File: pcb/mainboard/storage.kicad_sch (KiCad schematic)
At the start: 0 parts

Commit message: - Upgrade KiCad to latest version - Working on PM circuits - Initial USB Type-C support - Initial support for LCD
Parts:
- added C?: 100nF, Capacitor_SMD:C_0201_0603Metric, symbol Device:C
- added C?: 22uF, Capacitor_SMD:C_0603_1608Metric, symbol Device:C
- added C?: 470nF, Capacitor_SMD:C_0201_0603Metric, symbol Device:C
- added CARD?: MICRO_SD(TFC-WPAPR-08), footprint:TFC-WPAPR-08, symbol symbols:MICRO_SD(TFC-WPAPR-08)
- added J?: Bus_M.2_Socket_B, footprints:M2_BKEY, symbol Connector:Bus_M.2_Socket_B
- added R?: 100K, Capacitor_SMD:C_0402_1005Metric, symbol Device:R
- added R?: 0, Resistor_SMD:R_0402_1005Metric, symbol Device:R
- added U?: W25Q128JVP, Package_SON:WSON-8-1EP_6x5mm_P1.27mm_EP3.4x4.3mm, symbol Memory_Flash:W25Q32JVZP
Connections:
- new net: J?.11 (GND), J?.27 (GND), J?.3 (GND), J?.33 (GND), J?.39 (GND), J?.45 (GND), J?.5 (GND), J?.51 (GND), J?.57 (GND), J?.71 (GND), J?.73 (GND)
- new net: J?.2 (3.3V), J?.4 (3.3V), J?.70 (3.3V), J?.72 (3.3V), J?.74 (3.3V)
- new net: CARD?.5 (CLK/SCLK), R?.1
- new net +3V3: C?.1, C?.1, C?.2, CARD?.4 (VDD), R?.1, U?.8 (VCC)
- new net FSPI_1A_CS: R?.2, U?.1 (~CS)
- new net FSPI_1A_D0: U?.5 (DI(IO0))
- new net FSPI_1A_D1: U?.2 (DO(IO1))
- new net FSPI_1A_D2: U?.3 (IO2)
- new net FSPI_1A_D3: U?.7 (IO3)
- new net FSPI_1A_SCK: U?.6 (CLK)
- new net GND: C?.1, C?.2, C?.2, CARD?.10, CARD?.11, CARD?.12, CARD?.13, CARD?.6 (VSS), U?.4 (GND), U?.9 (EP)
- new net SD_CLK: R?.2
- new net SD_CMD: CARD?.3 (CMD/DI)
- new net SD_D0: CARD?.7 (DAT0/DO)
- new net SD_D1: CARD?.8 (DAT1/RES)
- new net SD_D2: CARD?.1 (DAT2/RES)
- new net SD_D3: CARD?.2 (CD/DAT3/CS)
- no-connect marks 0 -> 1
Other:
- note added: "Place close to MCU"

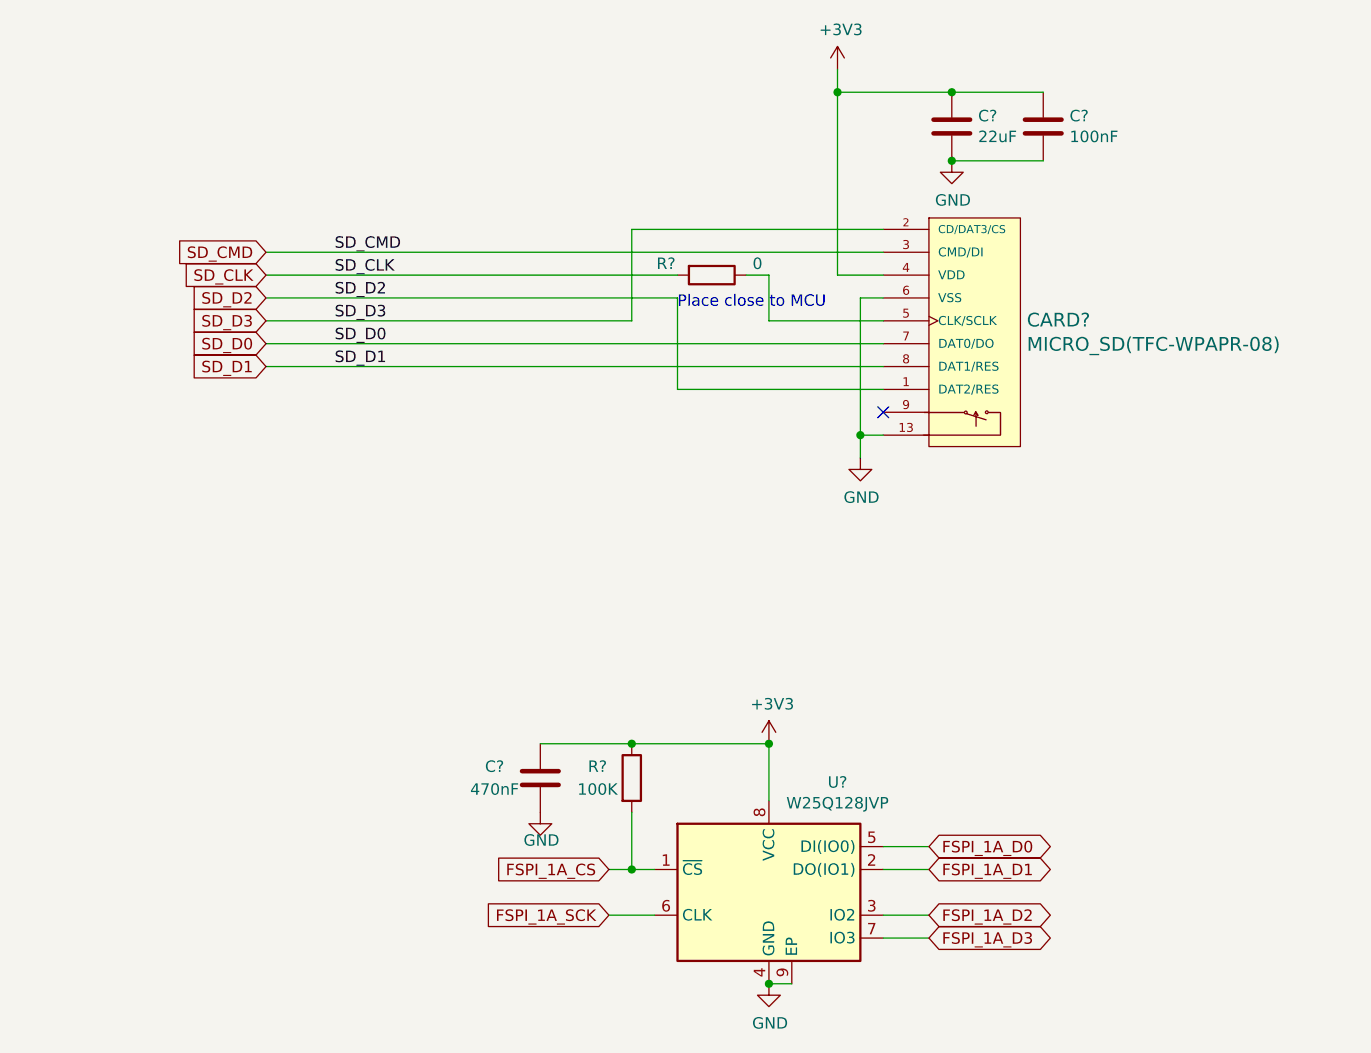
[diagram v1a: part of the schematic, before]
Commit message: - pcb: switch to imx7 for the prototype
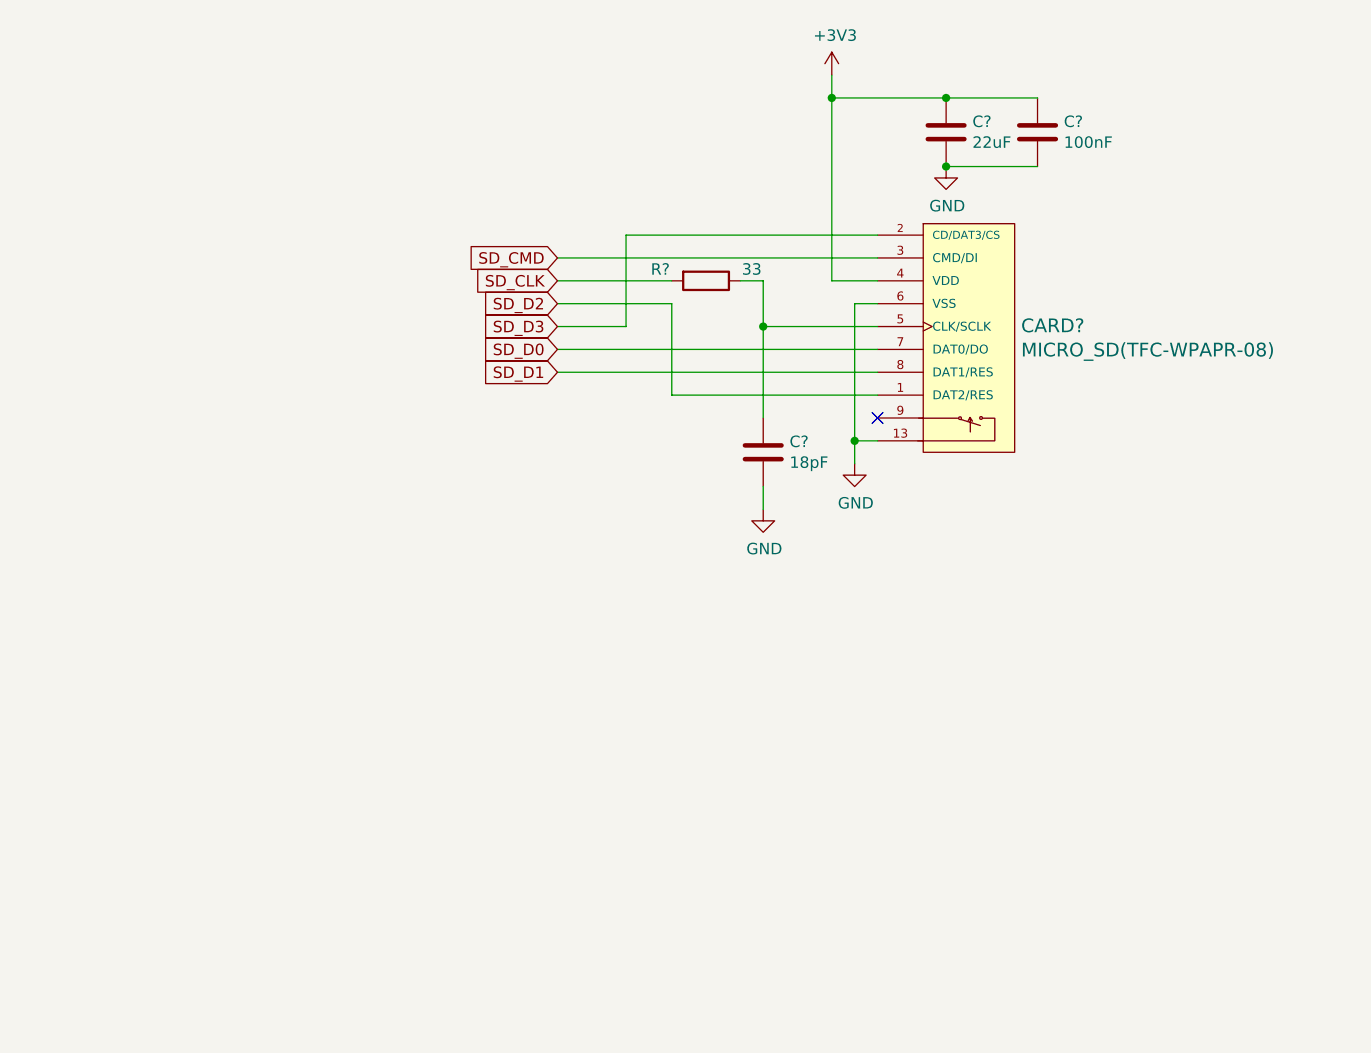
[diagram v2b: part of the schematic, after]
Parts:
- removed C?: 470nF, Capacitor_SMD:C_0201_0603Metric, symbol Device:C
- removed R?: 100K, Capacitor_SMD:C_0402_1005Metric, symbol Device:R
- removed U?: W25Q128JVP, Package_SON:WSON-8-1EP_6x5mm_P1.27mm_EP3.4x4.3mm, symbol Memory_Flash:W25Q32JVZP
- added C?: 18pF, Capacitor_SMD:C_0402_1005Metric, symbol Device:C
- R?: value 0 -> 33
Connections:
- net GND: now also C?.2
- net at CARD?.5 (CLK/SCLK), R?.1: now also C?.1
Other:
- note removed: "Place close to MCU"
- moved on the sheet: C?, CARD?, R?

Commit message: - pcb: working on r0p1 sch
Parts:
- removed J?: Bus_M.2_Socket_B, footprints:M2_BKEY, symbol Connector:Bus_M.2_Socket_B
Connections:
- net SD_CLK renamed SD1_CLK
- net SD_CMD renamed SD1_CMD
- net SD_D0 renamed SD1_DATA0
- net SD_D1 renamed SD1_DATA1
- net SD_D2 renamed SD1_DATA2
- net SD_D3 renamed SD1_DATA3
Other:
- moved on the sheet: C?, CARD?, R?

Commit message: - pcb: r0p1 sch draft
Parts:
- gave numbers to parts that had none: 5
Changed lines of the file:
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@@
 (kicad_sch (version 20210406) (generator eeschema)
-  (paper "A4")
+  (paper "A3")
   (title_block
     (title "Archer")
@@
   (symbol (lib_id "power:+3V3") (at 157.48 73.66 0) (unit 1)
     (in_bom yes) (on_board yes)
-    (property "Reference" "#PWR?" (id 0) (at 157.48 77.47 0)
+    (property "Reference" "#PWR0402" (id 0) (at 157.48 77.47 0)
       (effects (font (size 1.27 1.27)) hide)
     )
@@
   (symbol (lib_id "power:GND") (at 149.86 121.92 0) (unit 1)
     (in_bom yes) (on_board yes)
-    (property "Reference" "#PWR?" (id 0) (at 149.86 128.27 0)
+    (property "Reference" "#PWR0401" (id 0) (at 149.86 128.27 0)
       (effects (font (size 1.27 1.27)) hide)
     )
@@
   (symbol (lib_id "power:GND") (at 160.02 116.84 0) (unit 1)
     (in_bom yes) (on_board yes)
-    (property "Reference" "#PWR?" (id 0) (at 160.02 123.19 0)
+    (property "Reference" "#PWR0403" (id 0) (at 160.02 123.19 0)
       (effects (font (size 1.27 1.27)) hide)
     )
@@
   (symbol (lib_id "power:GND") (at 170.18 83.82 0) (unit 1)
     (in_bom yes) (on_board yes)
-    (property "Reference" "#PWR?" (id 0) (at 170.18 90.17 0)
+    (property "Reference" "#PWR0404" (id 0) (at 170.18 90.17 0)
       (effects (font (size 1.27 1.27)) hide)
     )
@@
   (symbol (lib_id "Device:R") (at 143.51 101.6 270) (unit 1)
     (in_bom yes) (on_board yes)
-    (property "Reference" "R?" (id 0) (at 138.43 100.33 90))
+    (property "Reference" "R401" (id 0) (at 138.43 100.33 90))
     (property "Value" "33" (id 1) (at 148.59 100.33 90))
     (property "Footprint" "Resistor_SMD:R_0402_1005Metric" (id 2) (at 143.51 99.822 90)
@@
   (symbol (lib_id "Device:C") (at 149.86 115.57 0) (unit 1)
     (in_bom yes) (on_board yes)
-    (property "Reference" "C?" (id 0) (at 152.781 114.4016 0)
+    (property "Reference" "C401" (id 0) (at 152.781 114.4016 0)
       (effects (font (size 1.27 1.27)) (justify left))
     )
@@
   (symbol (lib_id "Device:C") (at 170.18 80.01 0) (unit 1)
     (in_bom yes) (on_board yes)
-    (property "Reference" "C?" (id 0) (at 173.101 78.842 0)
+    (property "Reference" "C402" (id 0) (at 173.101 78.842 0)
       (effects (font (size 1.27 1.27)) (justify left))
     )
@@
   (symbol (lib_id "Device:C") (at 180.34 80.01 0) (unit 1)
     (in_bom yes) (on_board yes)
-    (property "Reference" "C?" (id 0) (at 183.261 78.842 0)
+    (property "Reference" "C403" (id 0) (at 183.261 78.842 0)
       (effects (font (size 1.27 1.27)) (justify left))
     )
@@
   (symbol (lib_id "symbols:MICRO_SD(TFC-WPAPR-08)") (at 170.18 104.14 0) (unit 1)
     (in_bom yes) (on_board yes)
-    (property "Reference" "CARD?" (id 0) (at 178.511 101.524 0)
+    (property "Reference" "J401" (id 0) (at 178.511 101.524 0)
       (effects (font (size 1.524 1.524)) (justify left))
     )

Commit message: - pcb: start r0p1 layout
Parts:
- C403: footprint Capacitor_SMD:C_0201_0603Metric -> Capacitor_SMD:C_0402_1005Metric
- J401: footprint footprint:TFC-WPAPR-08 -> footprints:TFC-WPAPR-08
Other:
- company: Copyright EI-2030 2021. -> Copyright EI-2030 2021. / Engineer: Wenting Zhang
- title: Archer -> Archer Mainboard
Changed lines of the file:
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@@
   (paper "A3")
   (title_block
-    (title "Archer")
-    (date "2021-04-26")
+    (title "Archer Mainboard")
+    (date "2021-05-05")
     (rev "R0.1 draft")
-    (company "Copyright EI-2030 2021.")
+    (company "Copyright EI-2030 2021. / Engineer: Wenting Zhang")
     (comment 2 "MERCHANTABILITY, SATISFACTORY QUALITY AND FITNESS FOR A PARTICULAR PURPOSE.")
-    (comment 3 "source is distributed WITHOUT ANY EXPRESS OR IMPLIED WARRANTY, INCLUDING OF")
-    (comment 4 "This source describes Open Hardware and is licensed under the CERN-OHL-S v2. This ")
+    (comment 3 "This source is distributed WITHOUT ANY EXPRESS OR IMPLIED WARRANTY, INCLUDING OF")
+    (comment 4 "This source describes Open Hardware and is licensed under the CERN-OHL-S v2.")
   )
   (junction (at 149.86 101.6) (diameter 0.9144) (color 0 0 0 0))
@@
       (effects (font (size 1.27 1.27)) (justify left))
     )
-    (property "Footprint" "Capacitor_SMD:C_0201_0603Metric" (id 2) (at 181.3052 83.82 0)
+    (property "Footprint" "Capacitor_SMD:C_0402_1005Metric" (id 2) (at 181.3052 83.82 0)
       (effects (font (size 1.27 1.27)) hide)
     )
@@
       (effects (font (size 1.524 1.524)) (justify left))
     )
-    (property "Footprint" "footprint:TFC-WPAPR-08" (id 2) (at 176.53 104.14 0)
+    (property "Footprint" "footprints:TFC-WPAPR-08" (id 2) (at 176.53 104.14 0)
       (effects (font (size 1.524 1.524)) hide)
     )

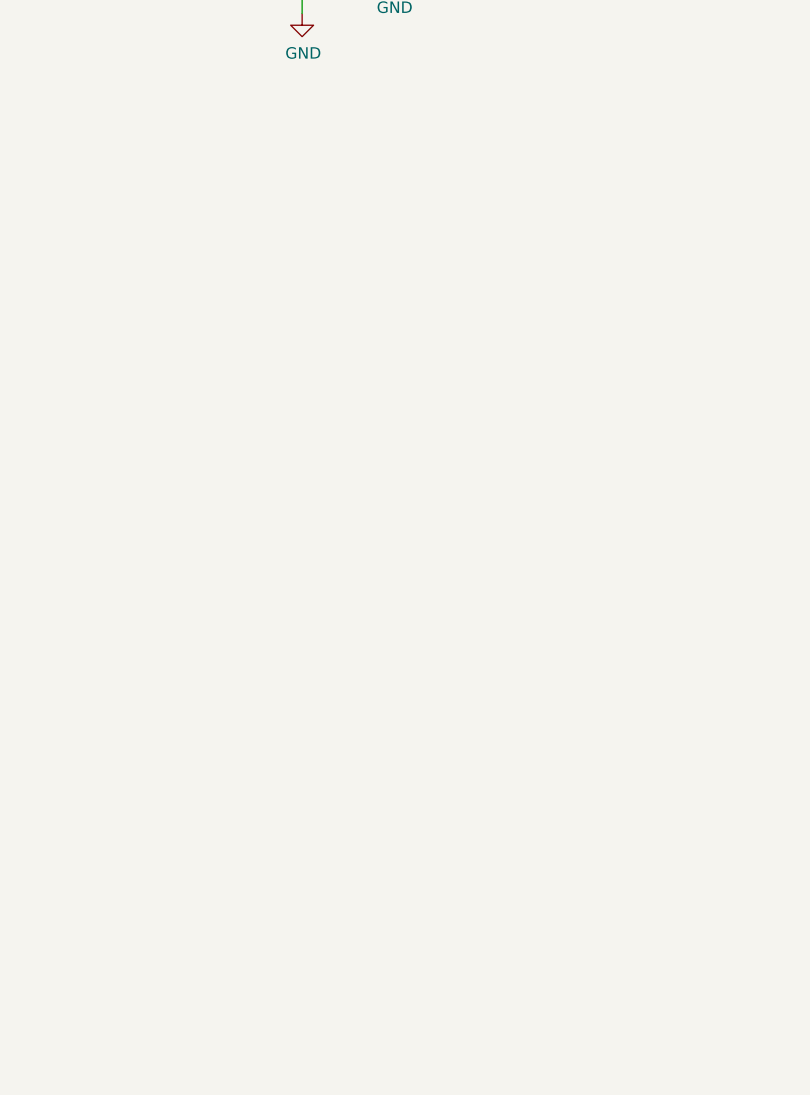
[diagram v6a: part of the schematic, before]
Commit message: - pcb: ddr layout
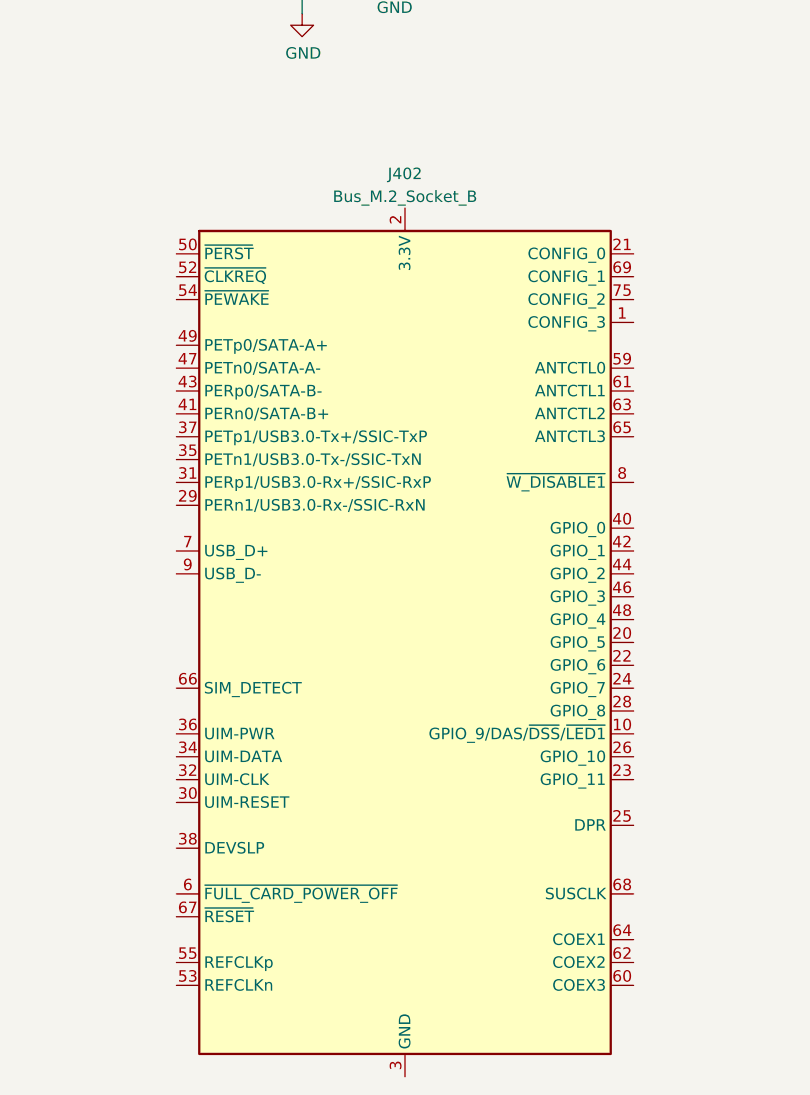
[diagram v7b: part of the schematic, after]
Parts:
- added J402: Bus_M.2_Socket_B, footprints:M2_BKEY, symbol Connector:Bus_M.2_Socket_B
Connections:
- new net: J402.11 (GND), J402.27 (GND), J402.3 (GND), J402.33 (GND), J402.39 (GND), J402.45 (GND), J402.5 (GND), J402.51 (GND), J402.57 (GND), J402.71 (GND), J402.73 (GND)
- new net: J402.2 (3.3V), J402.4 (3.3V), J402.70 (3.3V), J402.72 (3.3V), J402.74 (3.3V)
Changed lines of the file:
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@@
+    (pin "9")
+  )
+  (symbol (lib_id "Connector:Bus_M.2_Socket_B") (at 161.29 191.77 0) (unit 1)
+    (in_bom yes) (on_board yes) (fields_autoplaced)
+    (property "Reference" "J402" (id 0) (at 161.29 139.7 0))
+    (property "Value" "Bus_M.2_Socket_B" (id 1) (at 161.29 142.24 0))
+    (property "Footprint" "footprints:M2_BKEY" (id 2) (at 161.29 165.1 0)
+      (effects (font (size 1.27 1.27)) hide)
+    )
+    (property "Datasheet" "http://read.pudn.com/downloads794/doc/project/3133918/PCIe_M.2_Electromechanical_Spec_Rev1.0_Final_11012013_RS_Clean.pdf#page=154" (id 3) (at 161.29 165.1 0)
+      (effects (font (size 1.27 1.27)) hide)
+    )
+    (pin "1")
+    (pin "10")
+    (pin "11")
+    (pin "2")
+    (pin "20")
+    (pin "21")
+    (pin "22")
+    (pin "23")
+    (pin "24")
+    (pin "25")
+    (pin "26")
+    (pin "27")
+    (pin "28")
+    (pin "29")
+    (pin "3")
+    (pin "30")
+    (pin "31")
+    (pin "32")
+    (pin "33")
+    (pin "34")
+    (pin "35")
+    (pin "36")
+    (pin "37")
+    (pin "38")
+    (pin "39")
+    (pin "4")
+    (pin "40")
+    (pin "41")
+    (pin "42")
+    (pin "43")
+    (pin "44")
+    (pin "45")
+    (pin "46")
+    (pin "47")
+    (pin "48")
+    (pin "49")
+    (pin "5")
+    (pin "50")
+    (pin "51")
+    (pin "52")
+    (pin "53")
+    (pin "54")
+    (pin "55")
+    (pin "56")
+    (pin "57")
+    (pin "58")
+    (pin "59")
+    (pin "6")
+    (pin "60")
+    (pin "61")
+    (pin "62")
+    (pin "63")
+    (pin "64")
+    (pin "65")
+    (pin "66")
+    (pin "67")
+    (pin "68")
+    (pin "69")
+    (pin "7")
+    (pin "70")
+    (pin "71")
+    (pin "72")
+    (pin "73")
+    (pin "74")
+    (pin "75")
+    (pin "8")
     (pin "9")
   )

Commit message: - pcb: finishing layout r0p1
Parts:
- removed J402: Bus_M.2_Socket_B, footprints:M2_BKEY, symbol Connector:Bus_M.2_Socket_B
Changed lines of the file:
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@@
-    (pin "9")
-  )
-  (symbol (lib_id "Connector:Bus_M.2_Socket_B") (at 161.29 191.77 0) (unit 1)
-    (in_bom yes) (on_board yes) (fields_autoplaced)
-    (property "Reference" "J402" (id 0) (at 161.29 139.7 0))
-    (property "Value" "Bus_M.2_Socket_B" (id 1) (at 161.29 142.24 0))
-    (property "Footprint" "footprints:M2_BKEY" (id 2) (at 161.29 165.1 0)
-      (effects (font (size 1.27 1.27)) hide)
-    )
-    (property "Datasheet" "http://read.pudn.com/downloads794/doc/project/3133918/PCIe_M.2_Electromechanical_Spec_Rev1.0_Final_11012013_RS_Clean.pdf#page=154" (id 3) (at 161.29 165.1 0)
-      (effects (font (size 1.27 1.27)) hide)
-    )
-    (pin "1")
-    (pin "10")
-    (pin "11")
-    (pin "2")
-    (pin "20")
-    (pin "21")
-    (pin "22")
-    (pin "23")
-    (pin "24")
-    (pin "25")
-    (pin "26")
-    (pin "27")
-    (pin "28")
-    (pin "29")
-    (pin "3")
-    (pin "30")
-    (pin "31")
-    (pin "32")
-    (pin "33")
-    (pin "34")
-    (pin "35")
-    (pin "36")
-    (pin "37")
-    (pin "38")
-    (pin "39")
-    (pin "4")
-    (pin "40")
-    (pin "41")
-    (pin "42")
-    (pin "43")
-    (pin "44")
-    (pin "45")
-    (pin "46")
-    (pin "47")
-    (pin "48")
-    (pin "49")
-    (pin "5")
-    (pin "50")
-    (pin "51")
-    (pin "52")
-    (pin "53")
-    (pin "54")
-    (pin "55")
-    (pin "56")
-    (pin "57")
-    (pin "58")
-    (pin "59")
-    (pin "6")
-    (pin "60")
-    (pin "61")
-    (pin "62")
-    (pin "63")
-    (pin "64")
-    (pin "65")
-    (pin "66")
-    (pin "67")
-    (pin "68")
-    (pin "69")
-    (pin "7")
-    (pin "70")
-    (pin "71")
-    (pin "72")
-    (pin "73")
-    (pin "74")
-    (pin "75")
-    (pin "8")
     (pin "9")
   )
